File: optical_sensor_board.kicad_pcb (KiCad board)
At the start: 2 copper layers, 66 x 44 mm, 18 parts, among them J2 Conn_01x09_Socket, U1 PMW3389DM‐T3QU, U3 LM317L_SOT-89

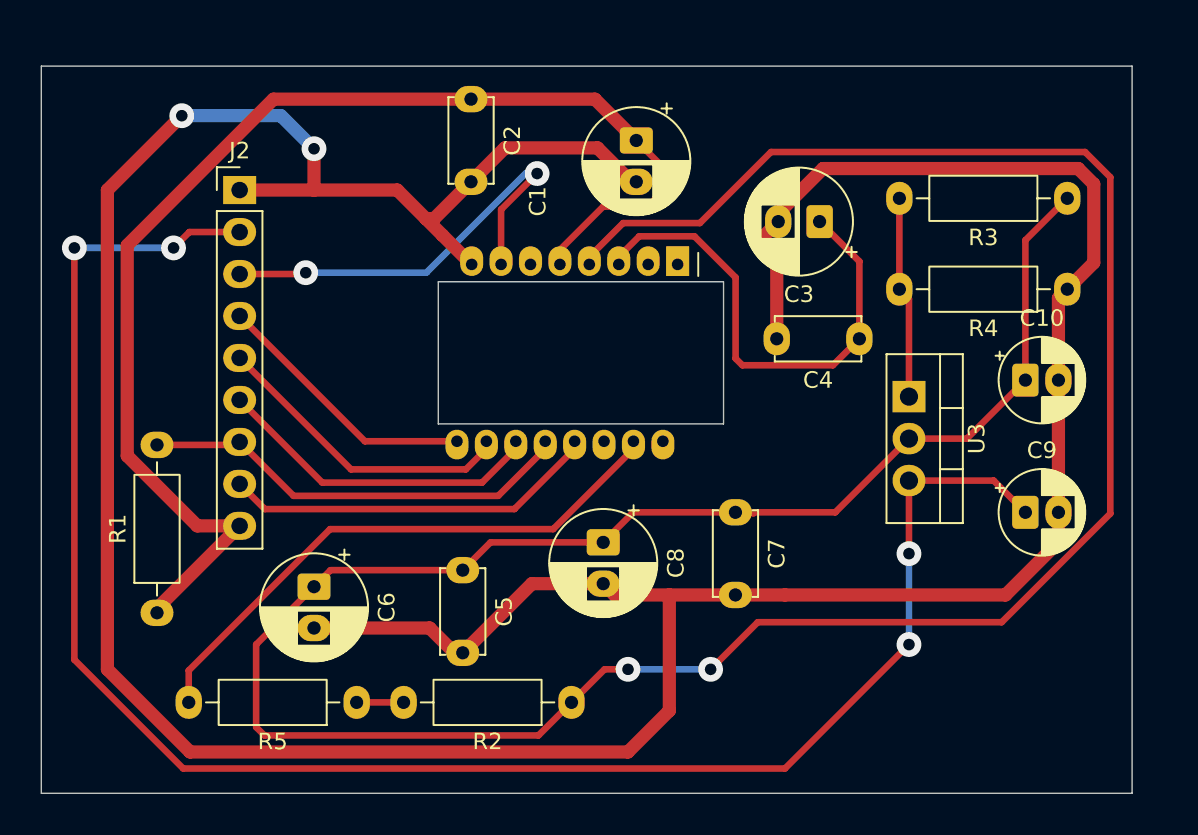
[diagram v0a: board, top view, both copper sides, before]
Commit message: Aggiunta copper-area + modifiche a schematico e master
Design:
 - Spostate le tracce sul bottom e i ponti sul top layer
 - Aggiunta la Copper Area sul bottom layer
 - Sistemate le serigrafie

Schematico:
 - Corretti gli errori del ERC aggiungendo i PWR_FLAG
 - Spostati i componenti per far si che si veda almeno un pezzettino di filo

Progetto:
 - Aggiunta la libreria dei footprint
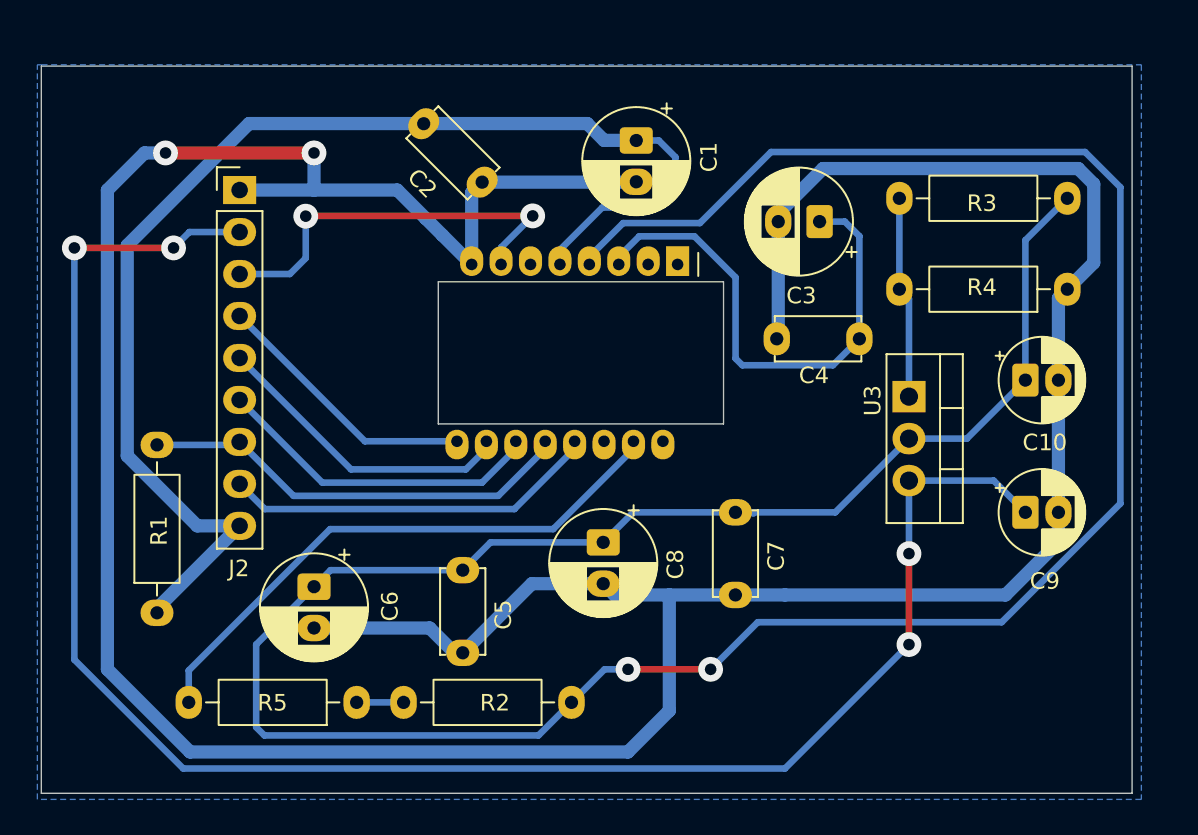
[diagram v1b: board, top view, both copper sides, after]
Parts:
- moved C2 3.22 mm to (135.1, 62.0), turned to -45 degrees
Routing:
- net GND: track 222.7 -> 219.0 mm
- net NRESET: track 26.9 -> 24.4 mm
- net VDDPIX: track 30.4 -> 31.3 mm
- net VDDIO: track 76.9 -> 77.6 mm
- net VDD: track 184.4 -> 184.9 mm
- added copper zone on B.Cu, net GND

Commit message: potentiometer footprint + potentiometer routing
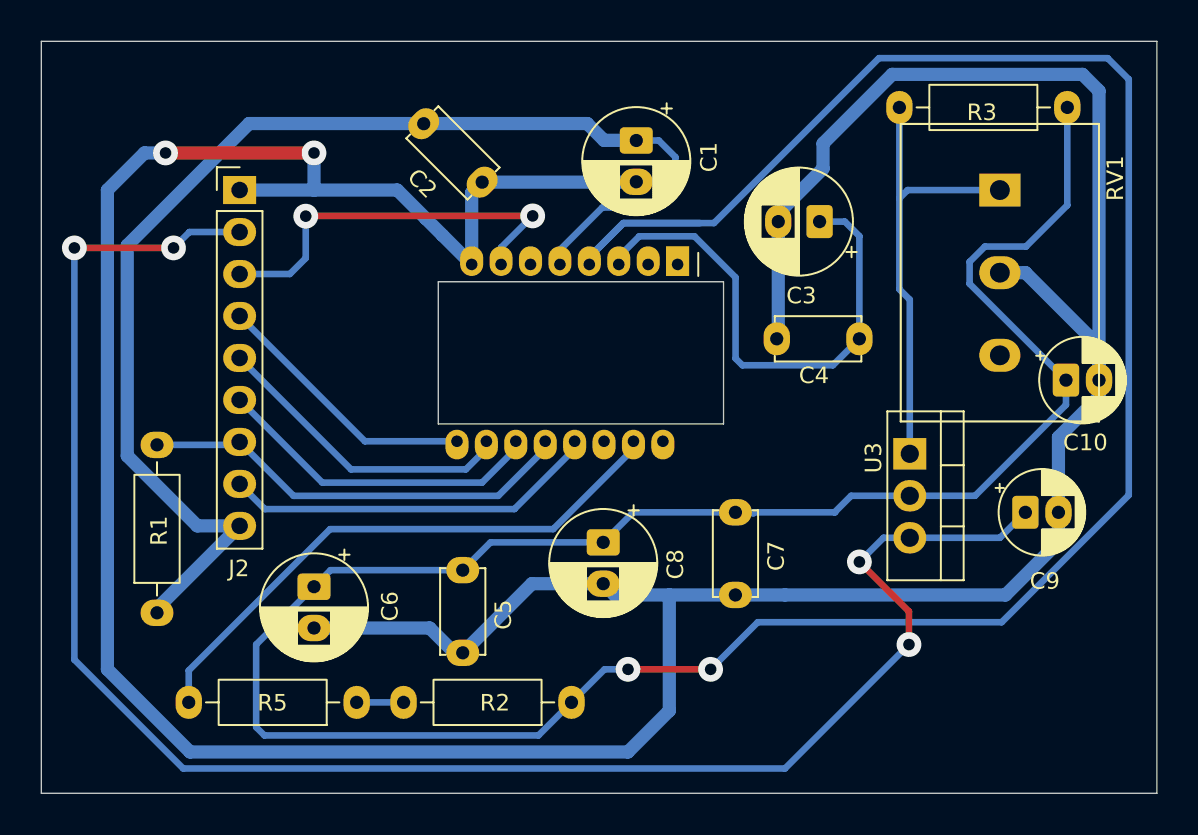
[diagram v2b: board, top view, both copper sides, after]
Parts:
- removed R4: 120R, MyOptical:LargePad_R_Axial_DIN0207_L6.3mm_D2.5mm_P10.16mm_Horizontal
- added RV1: 10K_p, MyOptical:LargerPad_P160, F.Cu at (170.0, 71.0)
- R3: value 240R -> 2K7
- moved R3 5.50 mm to (174.1, 61.0)
- moved U3 3.46 mm to (164.6, 82.0)
- moved C10 2.46 mm to (174.0, 77.5)
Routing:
- net VDD: track 184.9 -> 216.9 mm
- net GND: track 219.0 -> 238.3 mm
- net Net-(U3-ADJ): track 12.2 -> 27.5 mm
- removed copper zone on B.Cu, net GND
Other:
- board size 66 x 44 mm -> 67.5 x 45.5 mm

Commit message: copper area
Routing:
- added copper zone on B.Cu, net GND
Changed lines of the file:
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@@
 		(net 15)
+	)
+	(zone
+		(net 2)
+		(net_name "GND")
+		(layer "B.Cu")
+		(hatch edge 0.5)
+		(connect_pads
+			(clearance 0.5)
+		)
+		(min_thickness 0.25)
+		(filled_areas_thickness no)
+		(fill yes
+			(thermal_gap 0.5)
+			(thermal_bridge_width 0.5)
+		)
+		(polygon
+			(pts
+				(xy 111.5 56.5) (xy 180 56.5) (xy 180 103) (xy 111.5 103)
+			)
+		)
 	)
 	(embedded_fonts no)

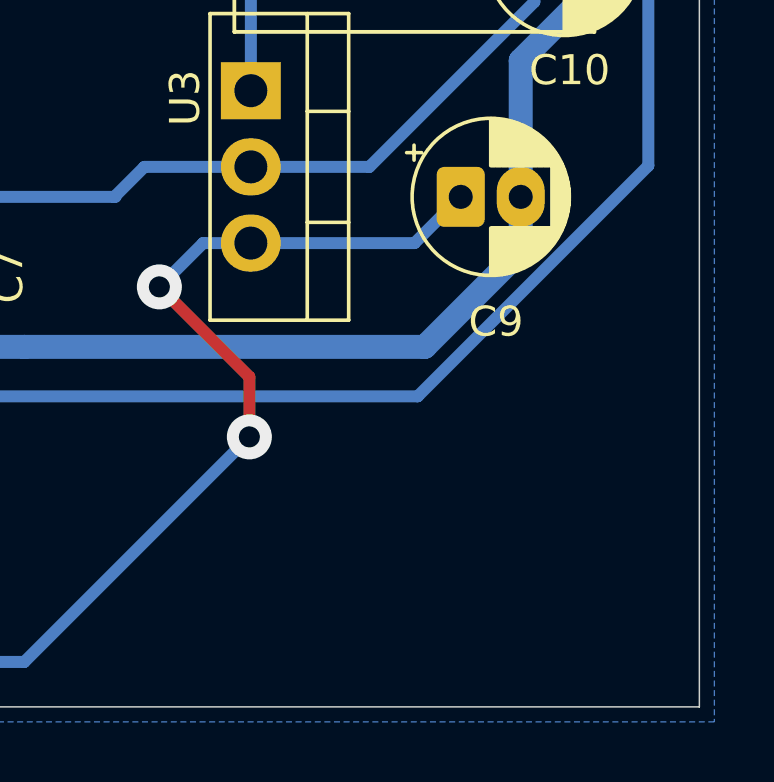
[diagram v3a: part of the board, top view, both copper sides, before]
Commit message: pmw3386Board RV1 text
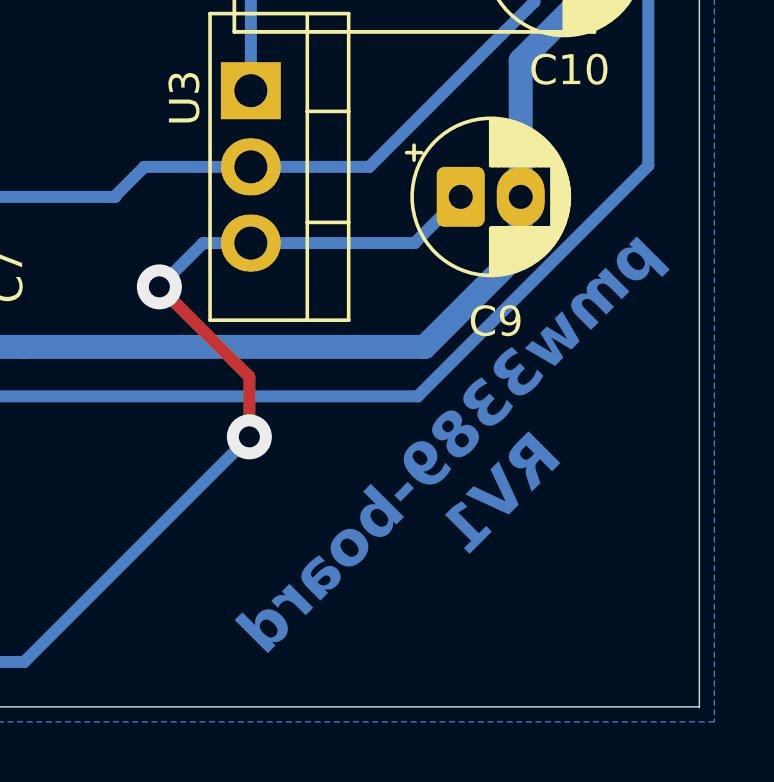
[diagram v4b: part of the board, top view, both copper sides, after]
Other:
- board text added: "pmw3389-board RV1"
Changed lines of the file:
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@@
 		(layer "Edge.Cuts")
+	)
+	(gr_text "pmw3389-board\nRV1\n"
+		(at 173.5 96 45)
+		(layer "B.Cu")
+		(effects
+			(font
+				(size 1.5 1.5)
+				(thickness 0.3)
+				(bold yes)
+			)
+			(justify bottom mirror)
+		)
 	)
 	(segment
